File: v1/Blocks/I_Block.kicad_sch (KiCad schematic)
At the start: 18 parts, among them IC19 TLV9351IDCKR, IC20 TLV9351IDCKR, IC21 TLV9351IDCKR, IC22 TLV9351IDCKR, IC23 TLV9351IDCKR, IC24 TLV9351IDCKR

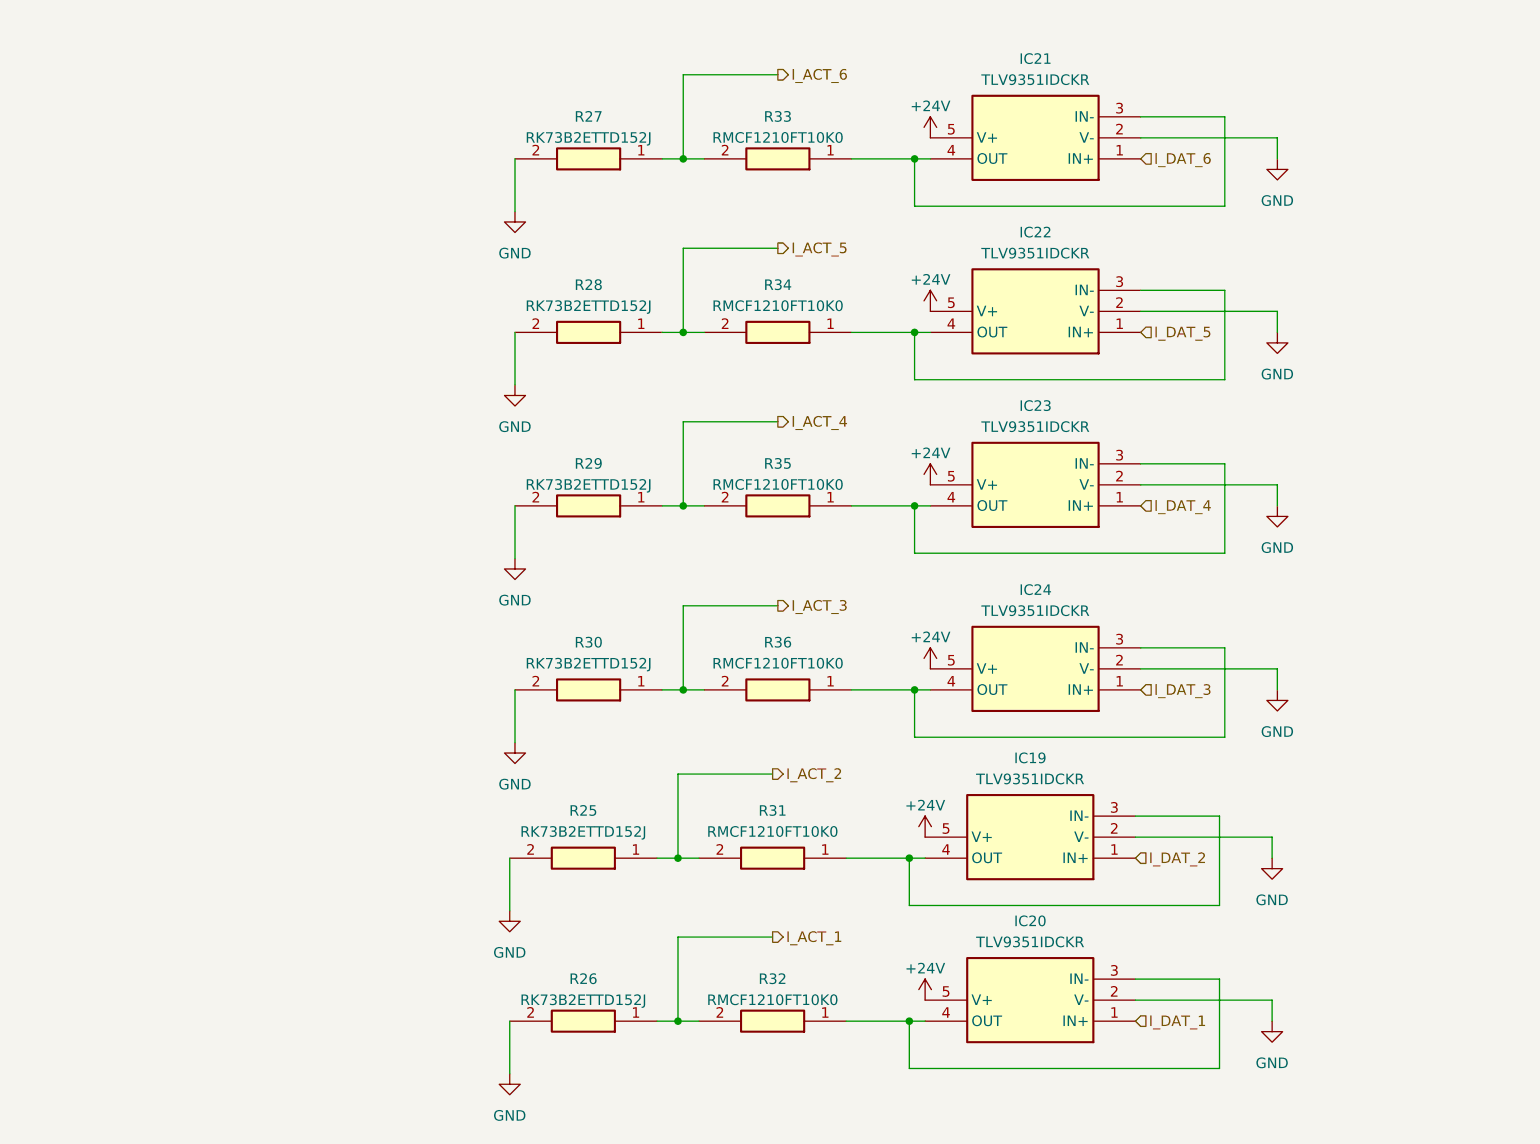
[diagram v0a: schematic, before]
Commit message: Update views, to make drawing sheets smaller where necessary
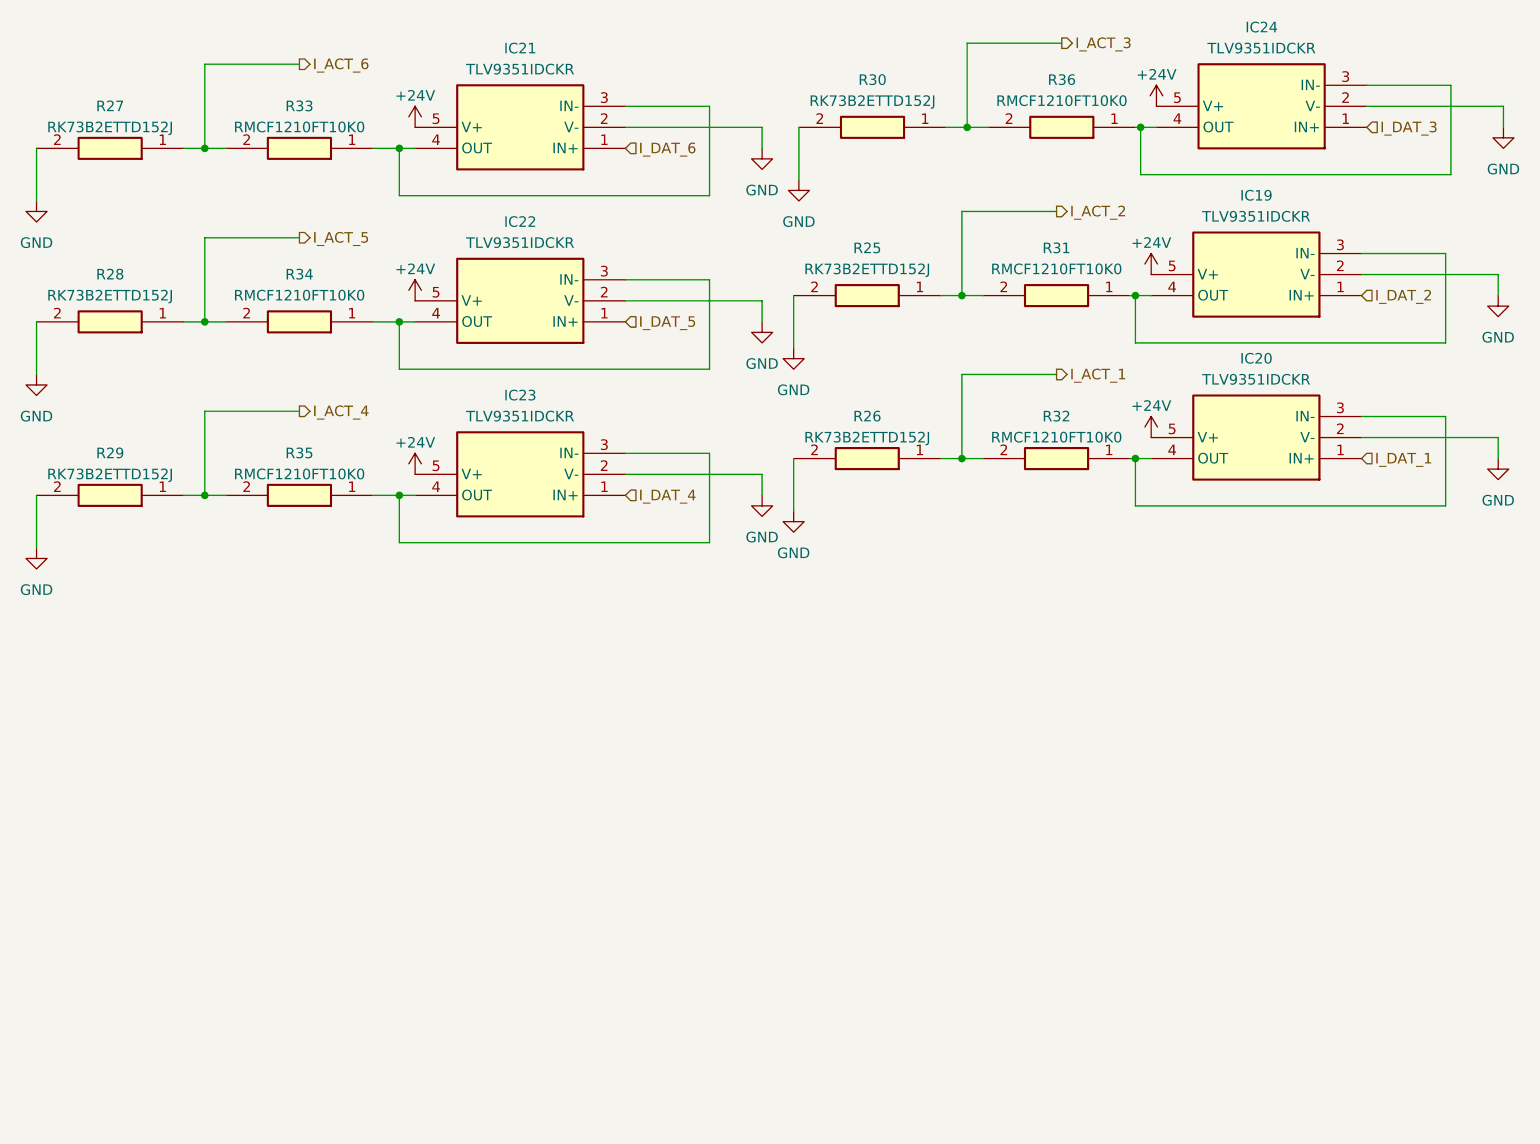
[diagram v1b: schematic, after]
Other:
- moved on the sheet: IC19, IC20, IC21, IC22, IC23, IC24, R25, R26, R27, R28, R29, R30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
